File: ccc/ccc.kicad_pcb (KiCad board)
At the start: 2 copper layers, 62 x 45 mm, 3 parts, among them J1 Conn_02x03_Odd_Even, U1 rt9013-33, U2 LTC3225

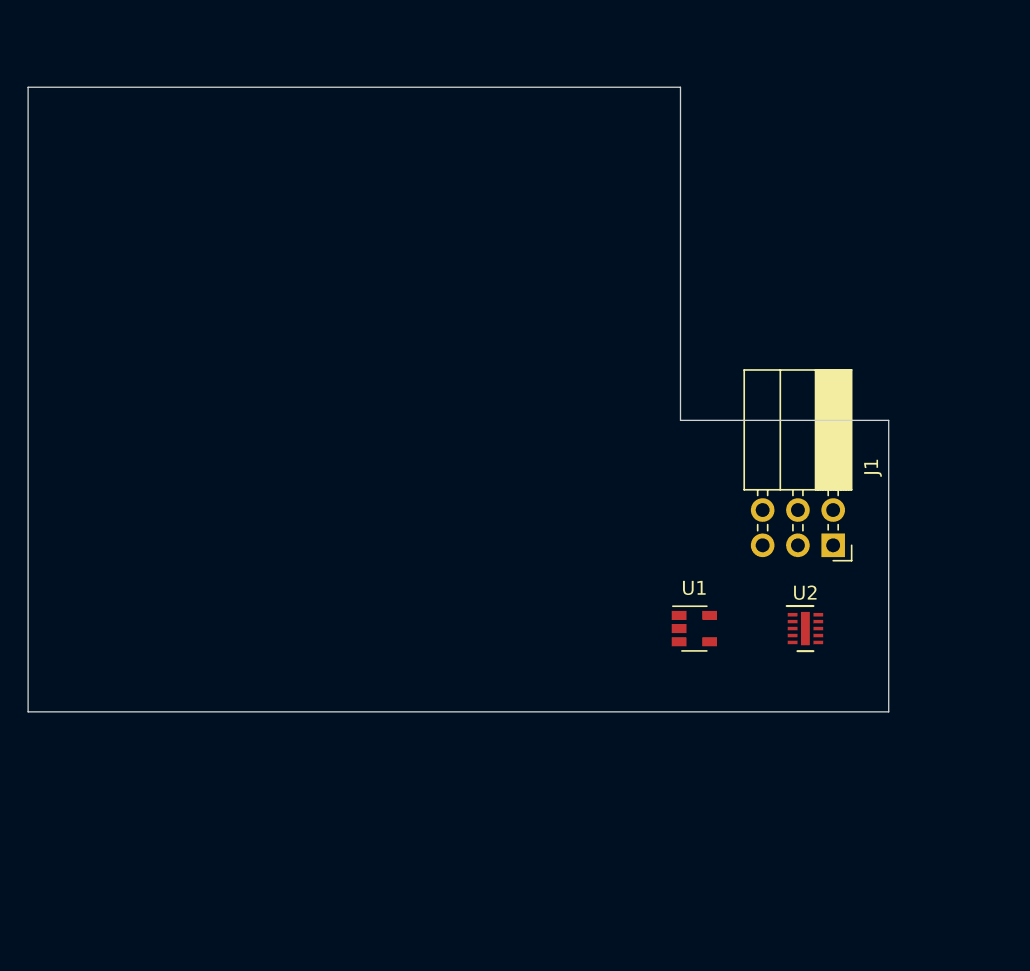
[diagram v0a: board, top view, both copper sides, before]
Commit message: Assigned footprints for stuff
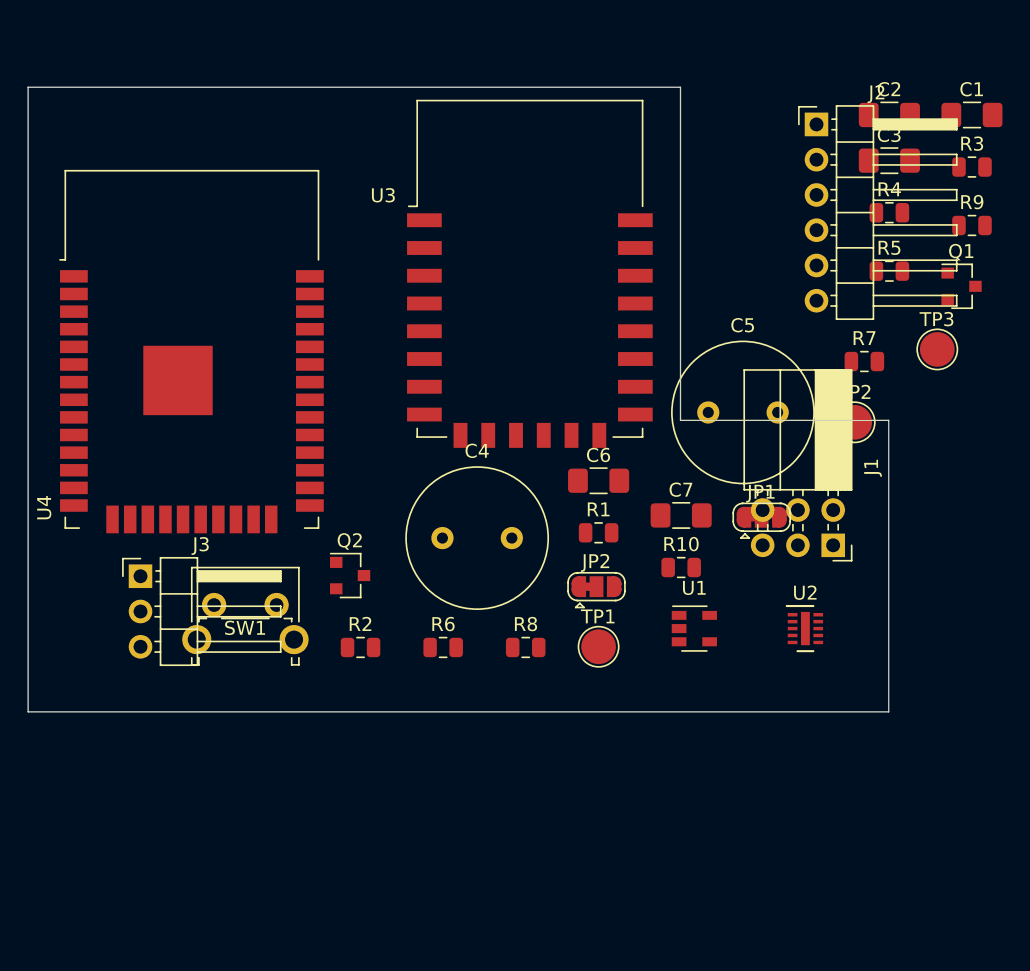
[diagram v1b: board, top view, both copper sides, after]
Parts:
- added C1: 2.2uf, Capacitor_SMD:C_1206_3216Metric_Pad1.42x1.75mm_HandSolder, F.Cu at (88.0, 22.0)
- added C2: 1uf, Capacitor_SMD:C_1206_3216Metric_Pad1.42x1.75mm_HandSolder, F.Cu at (82.0, 22.0)
- added C3: 0.1uf, Capacitor_SMD:C_1206_3216Metric_Pad1.42x1.75mm_HandSolder, F.Cu at (82.0, 25.3)
- added C4: 1.0f, Capacitor_THT:C_Radial_D10.0mm_H12.5mm_P5.00mm, F.Cu at (49.9, 52.5)
- added C5: 1.0f, Capacitor_THT:C_Radial_D10.0mm_H12.5mm_P5.00mm, F.Cu at (69.0, 43.4)
- added C6: 1uf(X7R), Capacitor_SMD:C_1206_3216Metric_Pad1.42x1.75mm_HandSolder, F.Cu at (61.1, 48.4)
- added C7: 1uf(X7R), Capacitor_SMD:C_1206_3216Metric_Pad1.42x1.75mm_HandSolder, F.Cu at (67.0, 50.9)
- added J2: Conn_01x06_Male, Connector_PinHeader_2.54mm:PinHeader_1x06_P2.54mm_Horizontal, F.Cu at (76.8, 22.7)
- added J3: Conn_01x03_Male, Connector_PinHeader_2.54mm:PinHeader_1x03_P2.54mm_Horizontal, F.Cu at (28.1, 55.2)
- added JP1: VSEL, Jumper:SolderJumper-3_P1.3mm_Bridged12_RoundedPad1.0x1.5mm, F.Cu at (72.8, 51.0)
- added JP2: FORCE, Jumper:SolderJumper-3_P1.3mm_Bridged12_RoundedPad1.0x1.5mm, F.Cu at (61.0, 56.0)
- added Q1: Q_NPN_BCE, Package_TO_SOT_SMD:SOT-23, F.Cu at (87.2, 34.3)
- added Q2: Q_NPN_BCE, Package_TO_SOT_SMD:SOT-23, F.Cu at (43.2, 55.2)
- added R1: 10k, Resistor_SMD:R_0805_2012Metric, F.Cu at (61.1, 52.1)
- added R10: 10k, Resistor_SMD:R_0805_2012Metric, F.Cu at (67.0, 54.6)
- added R2: 10k, Resistor_SMD:R_0805_2012Metric, F.Cu at (44.0, 60.4)
- added R3: 10k, Resistor_SMD:R_0805_2012Metric, F.Cu at (88.0, 25.8)
- added R4: 48k (51k), Resistor_SMD:R_0805_2012Metric, F.Cu at (82.0, 29.0)
- added R5: 10k, Resistor_SMD:R_0805_2012Metric, F.Cu at (82.0, 33.2)
- added R6: 10k, Resistor_SMD:R_0805_2012Metric, F.Cu at (49.9, 60.4)
- added R7: 10k, Resistor_SMD:R_0805_2012Metric, F.Cu at (80.2, 39.8)
- added R8: 10k, Resistor_SMD:R_0805_2012Metric, F.Cu at (55.9, 60.4)
- added R9: 10k, Resistor_SMD:R_0805_2012Metric, F.Cu at (88.0, 30.0)
- added SW1: RESET, Button_Switch_THT:SW_Tactile_SPST_Angled_PTS645Vx39-2LFS, F.Cu at (33.4, 57.3)
- added TP1: TestPoint, TestPoint:TestPoint_Pad_D2.5mm, F.Cu at (61.1, 60.3)
- added TP2: TestPoint, TestPoint:TestPoint_Pad_D2.5mm, F.Cu at (79.5, 44.1)
- added TP3: TestPoint, TestPoint:TestPoint_Pad_D2.5mm, F.Cu at (85.5, 38.9)
- added U3: ESP-12E, RF_Module:ESP-12E, F.Cu at (56.1, 33.1)
- added U4: ESP32-WROOM-32, RF_Module:ESP32-WROOM-32, F.Cu at (31.8, 41.9)
- U2: value LTC3225 -> LTC3225-1
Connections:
- J1 pad 1: GND -> VCC
- J1 pad 2: VCC -> GND
- J1 pad 3: TX -> KAM_RX
- J1 pad 4: RX -> KAM_TX
- U1 pad 1: Net-(U1-Pad1) -> VSS
- U1 pad 2: Net-(U1-Pad2) -> GND
- U1 pad 5: Net-(U1-Pad5) -> +3V3
- U2 pad 10: Net-(U2-Pad10) -> VSS
- U2 pad 4: Net-(U2-Pad4) -> VCC
- U2 pad 5: Net-(U2-Pad5) -> PGOOD
- U2 pad 8: Net-(U2-Pad8) -> GND
- U2 pad 9: Net-(U2-Pad9) -> VCC

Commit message: esp8266 is now removed from the schematic - some charging layout done
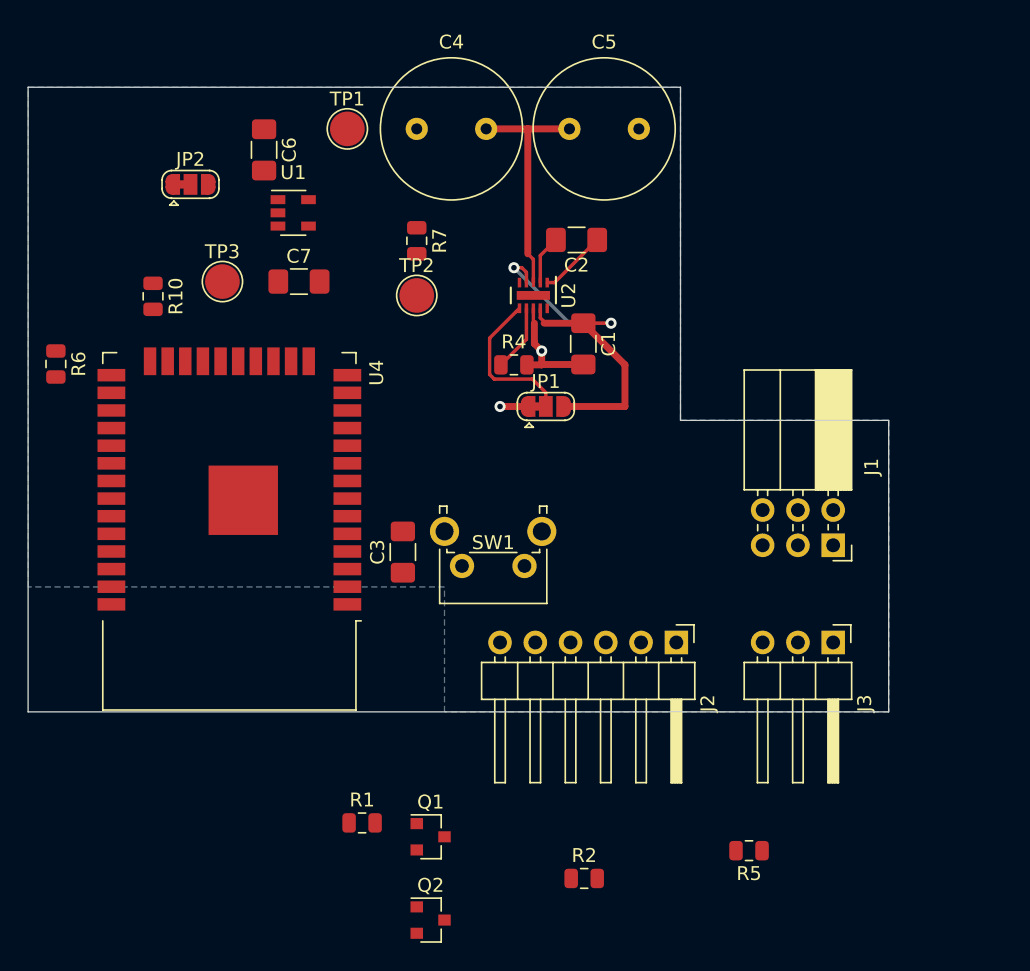
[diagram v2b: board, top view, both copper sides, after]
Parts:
- removed R3, R8, R9: 10k, Resistor_SMD:R_0805_2012Metric
- removed U3: ESP-12E, RF_Module:ESP-12E
- moved Q1 55.1 mm to (49.0, 74.0)
- moved TP3 51.7 mm to (34.0, 34.0)
- moved J3 50.1 mm to (78.0, 60.0), turned to 270 degrees
- moved C3 45.0 mm to (47.0, 53.5), turned to 90 degrees
- moved R5 43.0 mm to (71.9, 75.0), turned to 180 degrees
- moved R10 42.8 mm to (29.0, 35.1), turned to 270 degrees
- moved U1 41.6 mm to (39.1, 29.1)
- moved TP1 41.5 mm to (43.0, 23.0)
- moved JP2 41.2 mm to (31.7, 27.0)
- moved J2 38.7 mm to (66.7, 60.0), turned to 270 degrees
- moved R6 34.6 mm to (22.0, 39.9), turned to 270 degrees
- moved C6 33.9 mm to (37.0, 24.5), turned to 270 degrees
- moved R7 33.4 mm to (48.0, 31.1), turned to 270 degrees
- moved TP2 32.8 mm to (48.0, 35.0)
- moved C1 32.5 mm to (60.0, 38.5), turned to 270 degrees
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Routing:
- net VCC: track 0.00 -> 28.1 mm, vias 0 -> 2
- net Net-(C4-Pad2): track 0.00 -> 17.2 mm
- net Net-(JP1-Pad2): track 0.00 -> 11.2 mm
- net GND: track 0.00 -> 10.4 mm, vias 0 -> 2
- net Net-(C2-Pad1): track 0.00 -> 4.87 mm
- net Net-(R4-Pad1): track 0.00 -> 4.84 mm
- net Net-(C2-Pad2): track 0.00 -> 3.54 mm
- added copper zone on B.Cu, net GND

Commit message: Added flipflop - did some layout
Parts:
- removed C6, C7: 1uf(X7R), Capacitor_SMD:C_1206_3216Metric_Pad1.42x1.75mm_HandSolder
- removed JP2: FORCE, Jumper:SolderJumper-3_P1.3mm_Bridged12_RoundedPad1.0x1.5mm
- added U3: S7V8F3, Connector_PinHeader_2.54mm:PinHeader_1x04_P2.54mm_Vertical, F.Cu at (23.9, 23.4)
- U1: value rt9013-33 -> 74LVC1G373; footprint Package_TO_SOT_SMD:SOT-23-5 -> Package_TO_SOT_SMD:SOT-23-6_Handsoldering
- moved C4 17.8 mm to (48.0, 40.8)
- moved C5 17.8 mm to (59.0, 40.8)
- moved C2 15.6 mm to (65.9, 45.2), turned to 135 degrees
- moved JP1 14.2 mm to (63.6, 55.7)
- moved R4 14.2 mm to (61.4, 52.7)
- moved U2 14.2 mm to (62.8, 47.7)
- moved C1 14.2 mm to (66.3, 51.2)
- moved U1 5.33 mm to (34.1, 27.2)
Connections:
- C4 pad 1: VSS -> +4V
- R7 pad 1: VSS -> +4V
- TP1 pad 1: VSS -> +4V
- U1 pad 1: VSS -> PGOOD
- U1 pad 3: Net-(JP2-Pad2) -> +4V
- U1 pad 5: +3V3 -> +4V
- U2 pad 10: VSS -> +4V
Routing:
- net Net-(C4-Pad2): track 17.2 -> 6.00 mm
- net +4V: track 0.00 -> 7.49 mm
- net Net-(C2-Pad1): track 4.87 -> 3.37 mm

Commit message: Fully wired - needs some finish here and there
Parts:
- moved Q2 34.1 mm to (55.7, 46.6), turned to 270 degrees
- moved R2 31.6 mm to (50.0, 47.0), turned to 270 degrees
- moved R5 30.7 mm to (47.1, 57.0), turned to 0 degrees
- moved Q1 27.8 mm to (46.8, 46.3)
- moved R1 27.5 mm to (53.0, 47.0), turned to 270 degrees
- moved TP1 12.0 mm to (44.0, 35.0)
- moved TP3 9.22 mm to (25.0, 36.0)
- moved TP2 9.00 mm to (39.0, 35.0)
- moved U1 7.76 mm to (34.1, 35.0), turned to 180 degrees
- moved R7 6.01 mm to (42.1, 32.0), turned to 180 degrees
- moved C3 0.66 mm to (46.8, 52.9)
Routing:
- net +3V3: track 0.00 -> 74.7 mm, vias 0 -> 3
- net KAM_TX: track 0.00 -> 73.9 mm, vias 0 -> 1
- net KAM_RX: track 0.00 -> 66.9 mm, vias 0 -> 1
- net +4V: track 7.49 -> 66.6 mm, vias 0 -> 3
- net GPIO0: track 0.00 -> 37.9 mm
- net EXT_TX: track 0.00 -> 37.0 mm, vias 0 -> 1
- net PGOOD: track 0.00 -> 35.5 mm
- net EXT_RX: track 0.00 -> 33.5 mm, vias 0 -> 1
- net GND: track 10.4 -> 41.2 mm, vias 2 -> 8
- net RTS: track 0.00 -> 28.8 mm
- net RST: track 0.00 -> 18.9 mm
- net DTR: track 0.00 -> 17.2 mm
- net Net-(U1-Pad4): track 0.00 -> 15.1 mm
- net Net-(C4-Pad2): track 6.00 -> 17.0 mm
- net VCC: track 28.1 -> 38.6 mm
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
